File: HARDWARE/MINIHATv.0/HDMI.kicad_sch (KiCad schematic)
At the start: 3 parts, among them J3 HDMI_A, J4 DVI-D_Dual_Link, U4 TFP410PAP

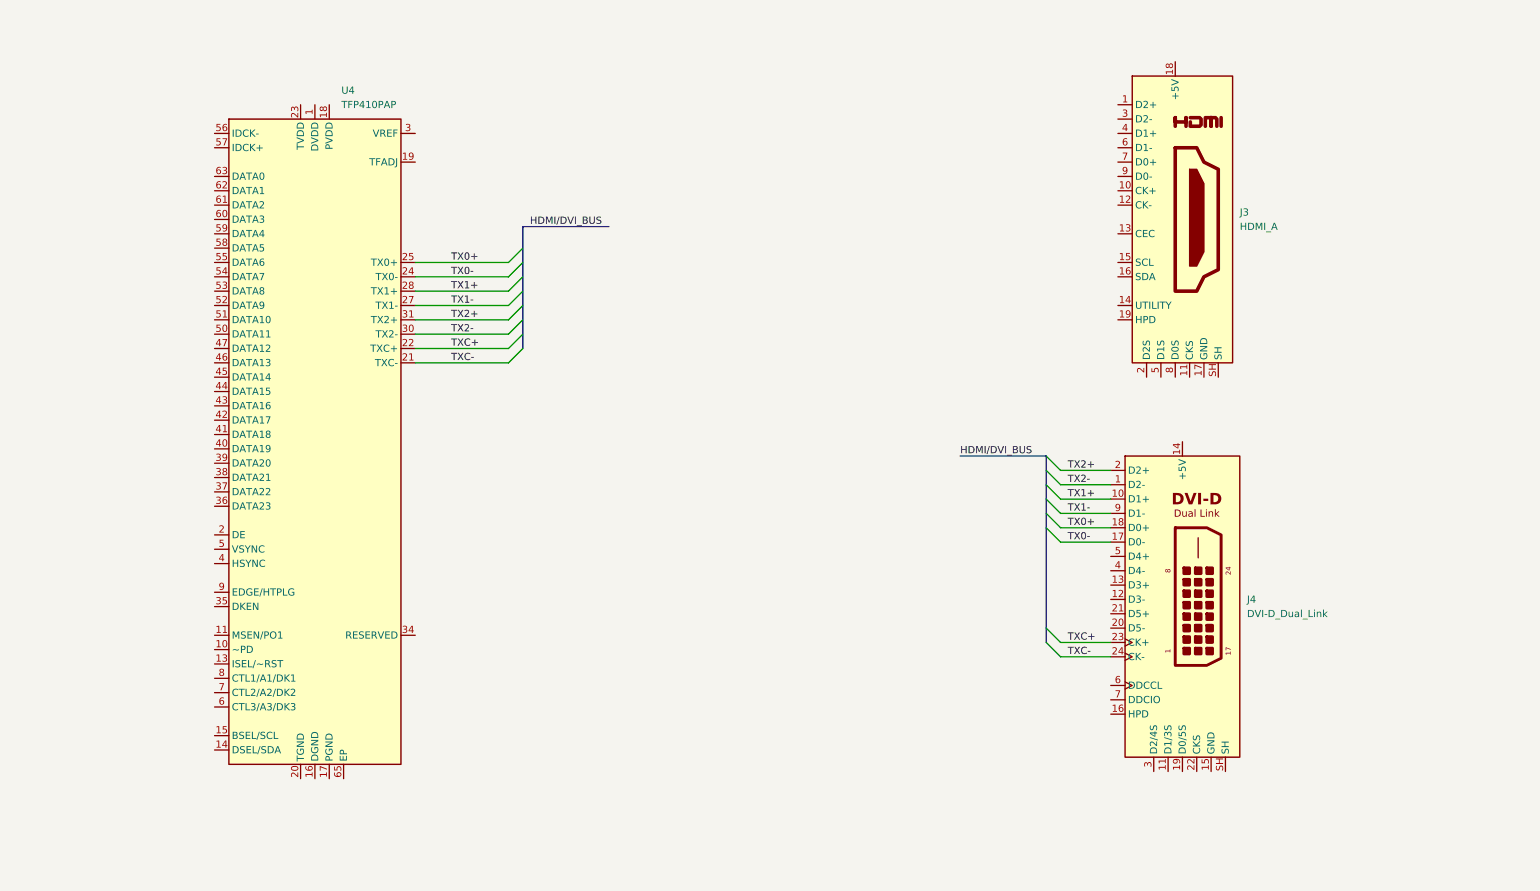
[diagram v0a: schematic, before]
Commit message: added beads and caps on drivers vdd
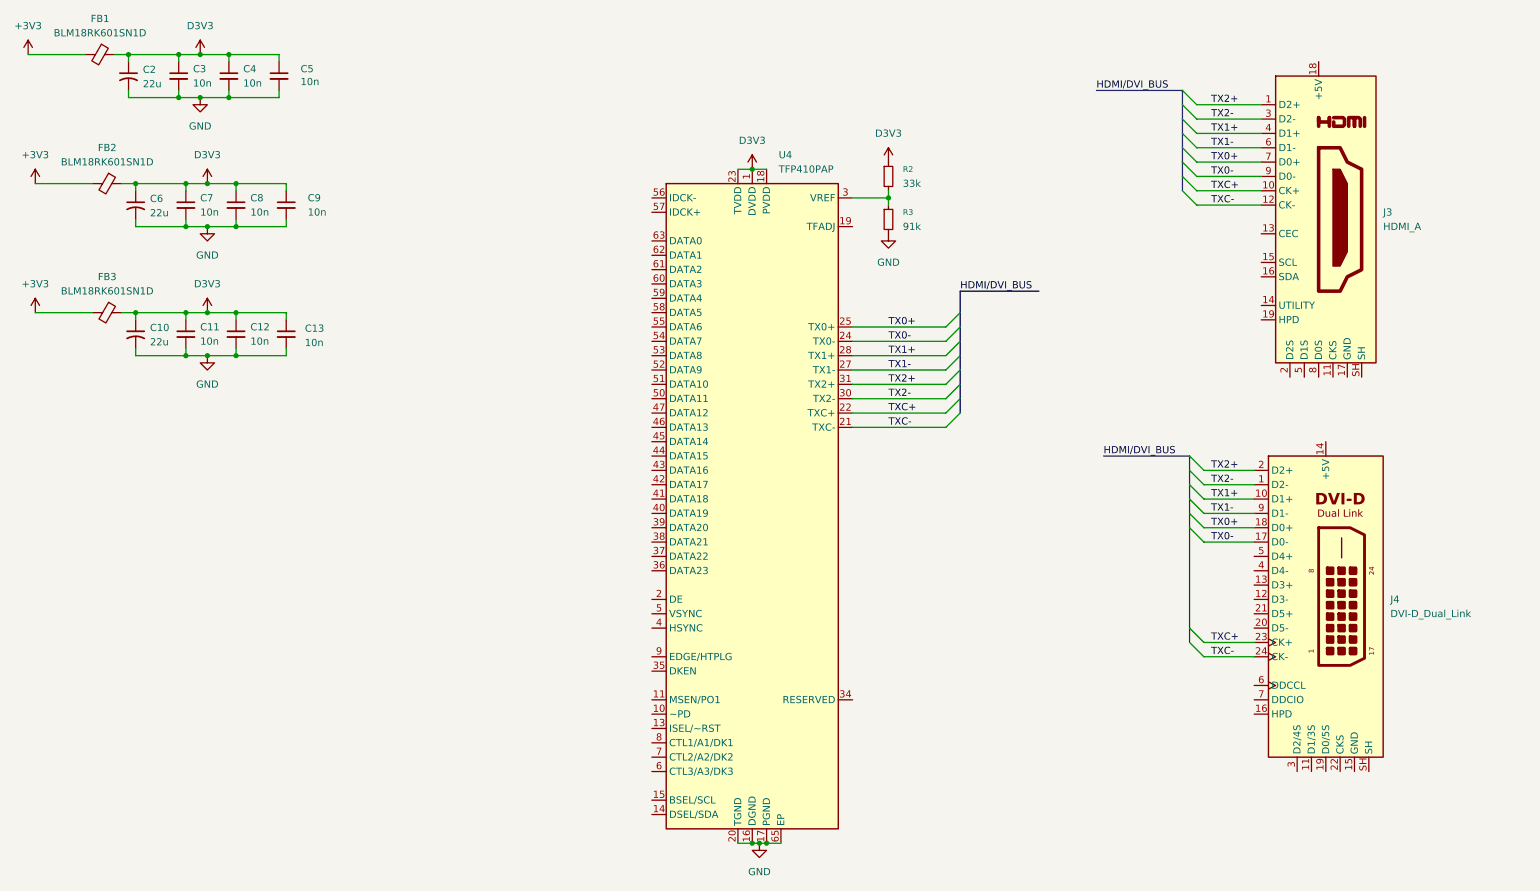
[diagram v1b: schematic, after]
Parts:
- added C10, C2, C6: 22u, symbol Device:C_Small_US
- added C11, C12, C13, C3, C4, C5, C7, C8, C9: 10n, symbol Device:C_Small
- added FB1, FB2, FB3: BLM18RK601SN1D, symbol Device:FerriteBead_Small
- added R2: 33k, symbol Device:R_Small
- added R3: 91k, symbol Device:R_Small
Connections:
- net TX0+: now also J3.7 (D0+)
- net TX0-: now also J3.9 (D0-)
- net TX1+: now also J3.4 (D1+)
- net TX1-: now also J3.6 (D1-)
- net TX2+: now also J3.1 (D2+)
- net TX2-: now also J3.3 (D2-)
- net TXC+: now also J3.10 (CK+)
- net TXC-: now also J3.12 (CK-)
- net D3V3: now reaches U4.1 (DVDD), U4.12 (DVDD), U4.33 (DVDD)
- net D3V3: now also U4.18 (PVDD), U4.23 (TVDD), U4.29 (TVDD), C10.1, C11.1, C12.1, C13.1, C2.1, C3.1, C4.1, C5.1, C6.1, C7.1, C8.1, C9.1, FB1.1, FB2.1, FB3.1, R2.1
- net GND: now reaches U4.16 (DGND), U4.48 (DGND), U4.64 (DGND)
- net GND: now also U4.17 (PGND), U4.20 (TGND), U4.26 (TGND), U4.32 (TGND), U4.65 (EP), C10.2, C11.2, C12.2, C13.2, C2.2, C3.2, C4.2, C5.2, C6.2, C7.2, C8.2, C9.2, R3.2
- net at U4.3 (VREF): now also R2.2, R3.1
- new net +3V3: FB1.2, FB2.2, FB3.2
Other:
- moved on the sheet: J3, J4, U4

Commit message: TFP to MCU connection added, TFP config pins tied
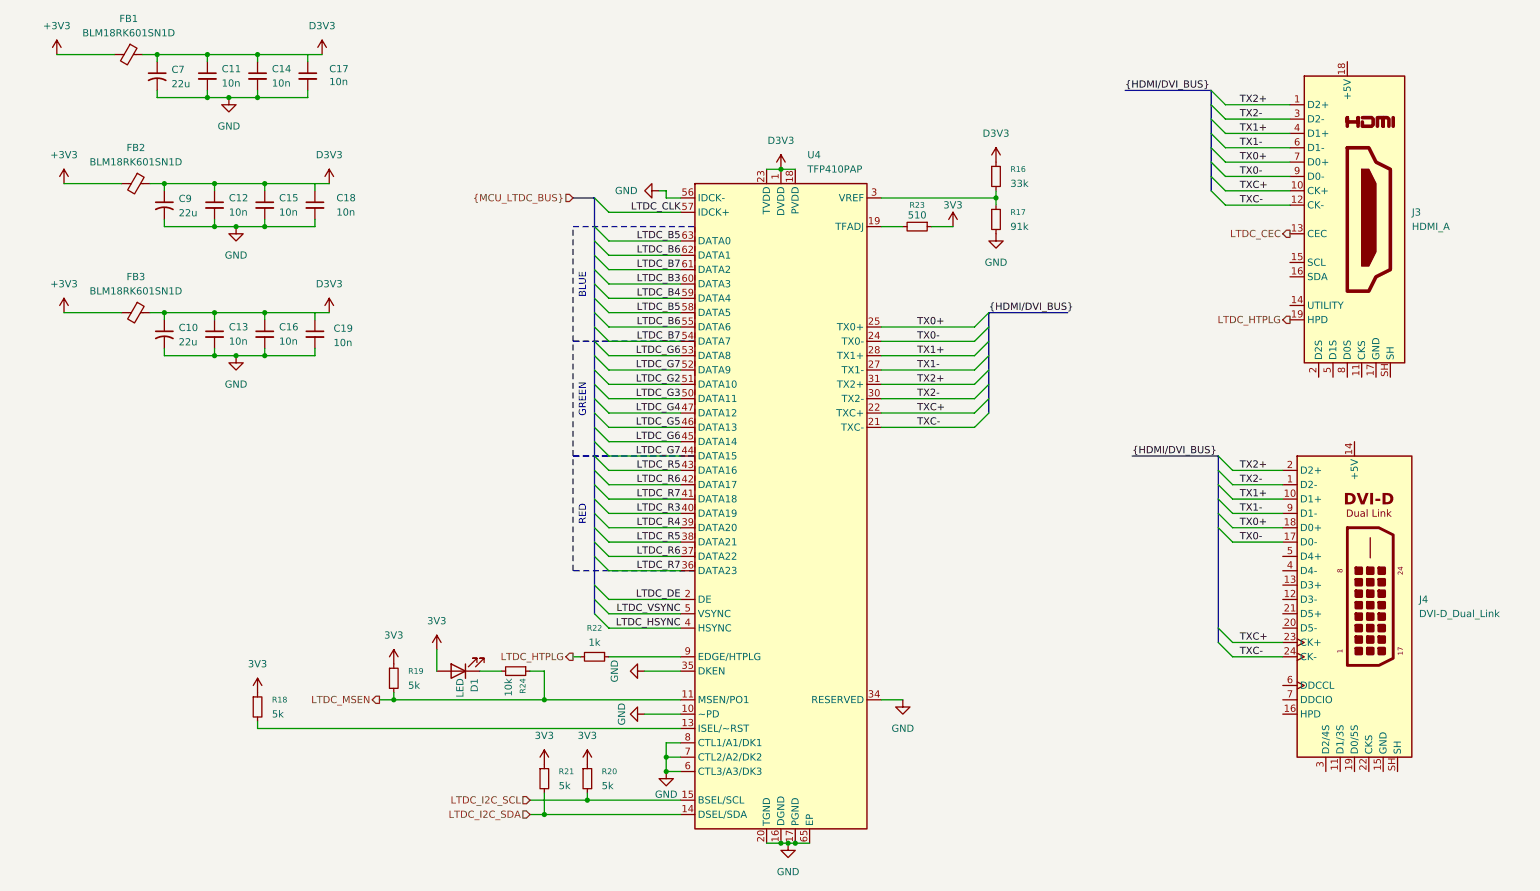
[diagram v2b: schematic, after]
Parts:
- added D1: LED, symbol Device:LED
- added R18, R19, R20, R21: 5k, symbol Device:R_Small
- added R22: 1k, symbol Device:R_Small
- added R23: 510, symbol Device:R_Small
- added R24: 10k, symbol Device:R_Small
- renumbered C3 to C11, C7 to C12, C11 to C13, C4 to C14, C8 to C15, C12 to C16, C5 to C17, C9 to C18, C13 to C19, C2 to C7, C6 to C9, R2 to R16, R3 to R17
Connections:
- net D3V3: no longer C17.1, C18.1, C19.1
- net GND: now also U4.10 (~PD), U4.34 (RESERVED), U4.35 (DKEN), U4.56 (IDCK-), U4.6 (CTL3/A3/DK3), U4.7 (CTL2/A2/DK2), U4.8 (CTL1/A1/DK1)
- net LTDC_MSEN: now reaches U4.11 (MSEN/PO1)
- net LTDC_MSEN: now also R19.2, R24.1
- net at U4.13 (ISEL/~RST): now also R18.2
- net LTDC_I2C_SDA: now reaches U4.14 (DSEL/SDA)
- net LTDC_I2C_SDA: now also R21.2
- net LTDC_I2C_SCL: now reaches U4.15 (BSEL/SCL)
- net LTDC_I2C_SCL: now also R20.2
- net at U4.19 (TFADJ): now also R23.2
- net LTDC_DE: now reaches U4.2 (DE)
- net LTDC_R7: now reaches U4.36 (DATA23)
- net LTDC_R7: now also U4.41 (DATA18)
- net LTDC_R6: now reaches U4.37 (DATA22)
- net LTDC_R6: now also U4.42 (DATA17)
- net LTDC_R5: now reaches U4.38 (DATA21)
- net LTDC_R5: now also U4.43 (DATA16)
- net LTDC_R4: now reaches U4.39 (DATA20)
- net LTDC_HSYNC: now reaches U4.4 (HSYNC)
- net LTDC_R3: now reaches U4.40 (DATA19)
- net LTDC_G7: now reaches U4.44 (DATA15)
- net LTDC_G7: now also U4.52 (DATA9)
- net LTDC_G6: now reaches U4.45 (DATA14)
- net LTDC_G6: now also U4.53 (DATA8)
- net LTDC_G5: now reaches U4.46 (DATA13)
- net LTDC_G4: now reaches U4.47 (DATA12)
- net LTDC_VSYNC: now reaches U4.5 (VSYNC)
- net LTDC_G3: now reaches U4.50 (DATA11)
- net LTDC_G2: now reaches U4.51 (DATA10)
- net LTDC_B7: now reaches U4.54 (DATA7)
- net LTDC_B7: now also U4.61 (DATA2)
- net LTDC_B6: now reaches U4.55 (DATA6)
- net LTDC_B6: now also U4.62 (DATA1)
- net LTDC_CLK: now reaches U4.57 (IDCK+)
- net LTDC_B5: now reaches U4.58 (DATA5)
- net LTDC_B5: now also U4.63 (DATA0)
- net LTDC_B4: now reaches U4.59 (DATA4)
- net LTDC_B3: now reaches U4.60 (DATA3)
- net at U4.9 (EDGE/HTPLG): now also R22.1
- net LTDC_CEC: now reaches J3.13 (CEC)
- net LTDC_HTPLG: now reaches J3.19 (HPD)
- net LTDC_HTPLG: now also R22.2
- new net: D1.1 (K), R24.2
- new net 3V3: D1.2 (A), R18.1, R19.1, R20.1, R21.1, R23.1
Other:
- moved on the sheet: C10, C11, C12, C13, C14, C15, C16, C17, C18, C19, C7, C9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

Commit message: deleted DVI, LTDC LSB tied GND
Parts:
- removed J4: DVI-D_Dual_Link, symbol Connector:DVI-D_Dual_Link
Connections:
- net GND: now also J3.17 (GND), J3.SH, U4.41 (DATA18), U4.42 (DATA17), U4.43 (DATA16), U4.52 (DATA9), U4.53 (DATA8), U4.61 (DATA2), U4.62 (DATA1), U4.63 (DATA0)
- net LTDC_B5: no longer U4.63 (DATA0)
- net LTDC_B6: no longer U4.62 (DATA1)
- net LTDC_B7: no longer U4.61 (DATA2)
- net LTDC_G6: no longer U4.53 (DATA8)
- net LTDC_G7: no longer U4.52 (DATA9)
- net LTDC_R5: no longer U4.43 (DATA16)
- net LTDC_R6: no longer U4.42 (DATA17)
- net LTDC_R7: no longer U4.41 (DATA18)
- net 5V: now reaches J3.18 (+5V)
- no-connect marks 0 -> 1
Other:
- moved on the sheet: J3

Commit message: HDMI socked connection finished
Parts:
- R24: value 10k -> 120
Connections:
- net GND: now also J3.11 (CKS), J3.2 (D2S), J3.5 (D1S), J3.8 (D0S)
- net HDMI_SCL: now reaches J3.15 (SCL)
- net HDMI_SDA: now reaches J3.16 (SDA)
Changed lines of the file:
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@@
 	)
 	(junction
-		(at 265.43 121.92)
-		(diameter 0)
-		(color 0 0 0 0)
-	)
-	(junction
 		(at 53.34 55.88)
 		(diameter 0)
@@
 	)
 	(junction
+		(at 259.08 121.92)
+		(diameter 0)
+		(color 0 0 0 0)
+	)
+	(junction
 		(at 60.96 33.02)
 		(diameter 0)
@@
 	)
 	(junction
+		(at 264.16 121.92)
+		(diameter 0)
+		(color 0 0 0 0)
+	)
+	(junction
+		(at 256.54 121.92)
+		(diameter 0)
+		(color 0 0 0 0)
+	)
+	(junction
 		(at 62.23 48.26)
 		(diameter 0)
@@
 	)
 	(junction
+		(at 260.35 121.92)
+		(diameter 0)
+		(color 0 0 0 0)
+	)
+	(junction
 		(at 111.76 160.02)
 		(diameter 0)
@@
 	)
 	(junction
+		(at 261.62 121.92)
+		(diameter 0)
+		(color 0 0 0 0)
+	)
+	(junction
 		(at 135.89 78.74)
 		(diameter 0)
@@
 	(wire
 		(pts
+			(xy 259.08 121.92) (xy 260.35 121.92)
+		)
+		(stroke
+			(width 0)
+			(type default)
+		)
+	)
+	(wire
+		(pts
 			(xy 119.38 157.48) (xy 135.89 157.48)
 		)
@@
 	(wire
 		(pts
+			(xy 254 121.92) (xy 256.54 121.92)
+		)
+		(stroke
+			(width 0)
+			(type default)
+		)
+	)
+	(wire
+		(pts
 			(xy 60.96 143.51) (xy 60.96 144.78)
 		)
@@
 	(wire
 		(pts
-			(xy 264.16 121.92) (xy 265.43 121.92)
-		)
-		(stroke
-			(width 0)
-			(type default)
-		)
-	)
-	(wire
-		(pts
-			(xy 265.43 121.92) (xy 266.7 121.92)
-		)
-		(stroke
-			(width 0)
-			(type default)
-		)
-	)
-	(wire
-		(pts
 			(xy 111.76 134.62) (xy 111.76 139.7)
 		)
@@
 	(wire
 		(pts
+			(xy 234.95 111.76) (xy 248.92 111.76)
+		)
+		(stroke
+			(width 0)
+			(type default)
+		)
+	)
+	(wire
+		(pts
 			(xy 171.45 76.2) (xy 187.96 76.2)
 		)
@@
 	(wire
 		(pts
+			(xy 260.35 121.92) (xy 266.7 121.92)
+		)
+		(stroke
+			(width 0)
+			(type default)
+		)
+	)
+	(wire
+		(pts
+			(xy 260.35 124.46) (xy 260.35 121.92)
+		)
+		(stroke
+			(width 0)
+			(type default)
+		)
+	)
+	(wire
+		(pts
 			(xy 135.89 50.8) (xy 133.35 50.8)
 		)
@@
 	(wire
 		(pts
+			(xy 256.54 121.92) (xy 259.08 121.92)
+		)
+		(stroke
+			(width 0)
+			(type default)
+		)
+	)
+	(wire
+		(pts
 			(xy 123.19 106.68) (xy 135.89 106.68)
 		)
@@
 	)
 	(label "LTDC_HTPLG"
-		(at 248.92 111.76 180)
+		(at 234.95 111.76 0)
 		(effects
 			(font
 				(size 1.27 1.27)
 			)
-			(justify right bottom)
+			(justify left bottom)
 		)
 	)
@@
 		)
 	)
+	(hierarchical_label "HDMI_SDA"
+		(shape output)
+		(at 248.92 104.14 180)
+		(effects
+			(font
+				(size 1.27 1.27)
+			)
+			(justify right)
+		)
+	)
 	(hierarchical_label "{MCU_LTDC_BUS}"
 		(shape input)
@@
 		)
 	)
+	(hierarchical_label "HDMI_SCL"
+		(shape output)
+		(at 248.92 101.6 180)
+		(effects
+			(font
+				(size 1.27 1.27)
+			)
+			(justify right)
+		)
+	)
 	(hierarchical_label "LTDC_I2C_SDA"
 		(shape input)
@@
 			)
 		)
-		(property "Value" "10k"
+		(property "Value" "120"
 			(at 105.41 135.89 0)
 			(show_name no)
@@
 	(symbol
 		(lib_id "power:GND")
-		(at 265.43 121.92 0)
+		(at 260.35 124.46 0)
 		(unit 1)
 		(body_style 1)
@@
 		(fields_autoplaced yes)
 		(property "Reference" "#PWR033"
-			(at 265.43 128.27 0)
+			(at 260.35 130.81 0)
 			(hide yes)
 			(show_name no)
@@
 		)
 		(property "Value" "GND"
-			(at 265.43 127 0)
+			(at 260.35 129.54 0)
 			(show_name no)
 			(do_not_autoplace no)
@@
 		)
 		(property "Footprint" ""
-			(at 265.43 121.92 0)
+			(at 260.35 124.46 0)
 			(hide yes)
 			(show_name no)
@@
 		)
 		(property "Datasheet" ""
-			(at 265.43 121.92 0)
+			(at 260.35 124.46 0)
 			(hide yes)
 			(show_name no)
@@
 		)
 		(property "Description" "Power symbol creates a global label with name \"GND\" , ground"
-			(at 265.43 121.92 0)
+			(at 260.35 124.46 0)
 			(hide yes)
 			(show_name no)

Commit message: added i2c for hdmi
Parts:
- D7: renamed from D1; value LED -> LED B
- renumbered C7 to C21, C9 to C22, C10 to C23, C11 to C24, C12 to C25, C13 to C26, C14 to C27, C15 to C28, C16 to C29, C17 to C30, C18 to C31, C19 to C32, FB1 to FB2, FB2 to FB3, FB3 to FB4, J3 to J4, R18 to R29, R19 to R30, R24 to R31, R21 to R32, R20 to R33, R22 to R34, R23 to R35, R16 to R36, R17 to R37, U4 to U6
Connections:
- net 5V renamed +5V

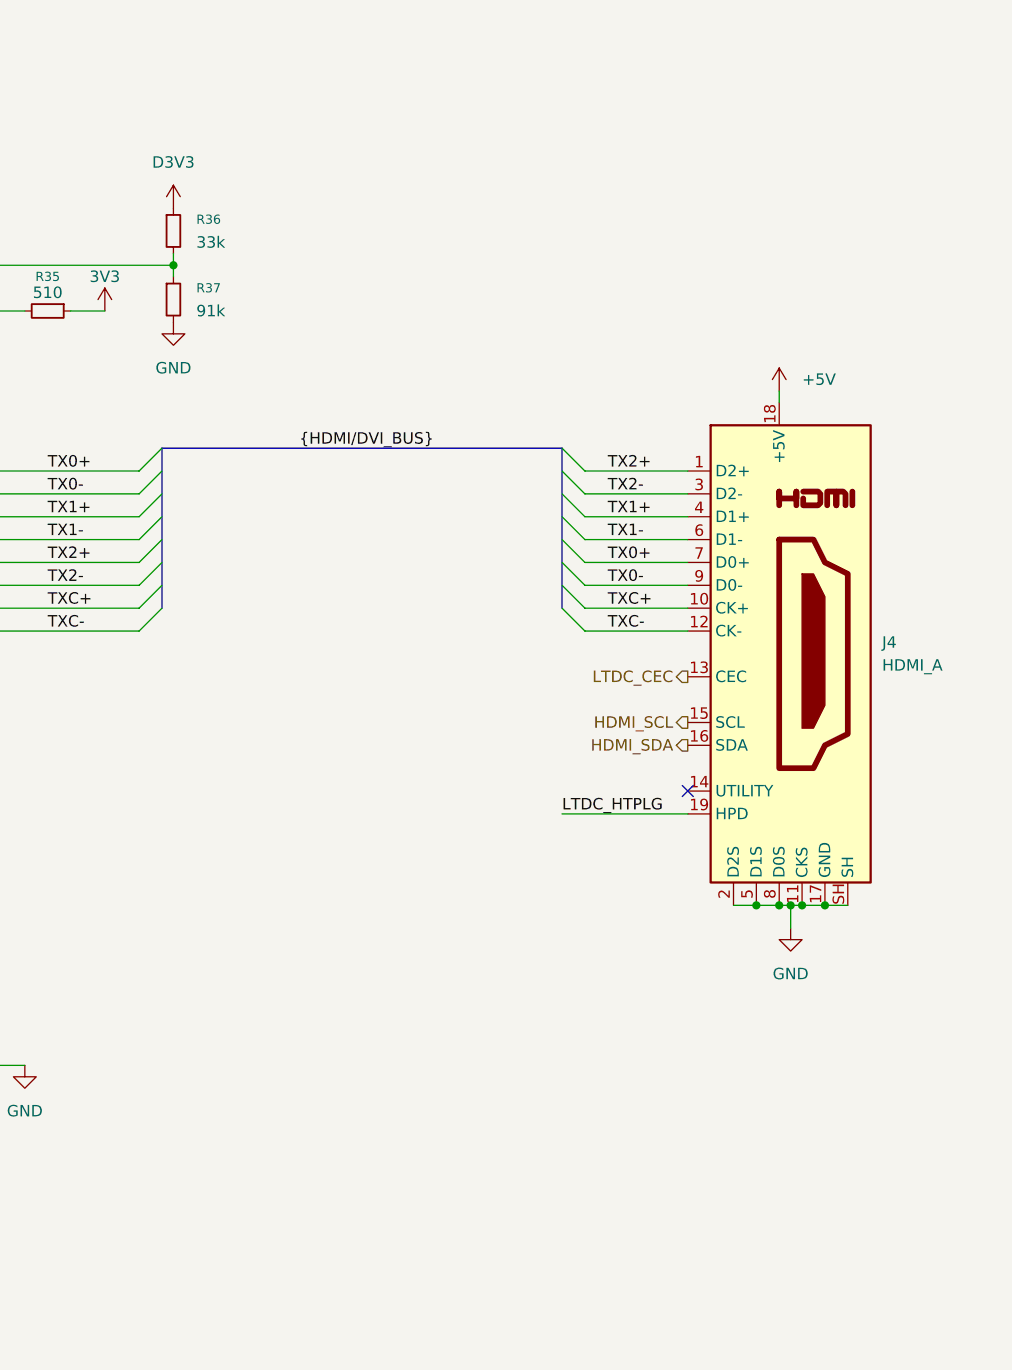
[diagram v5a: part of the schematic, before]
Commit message: connecting i2c and uart bt/hdmi
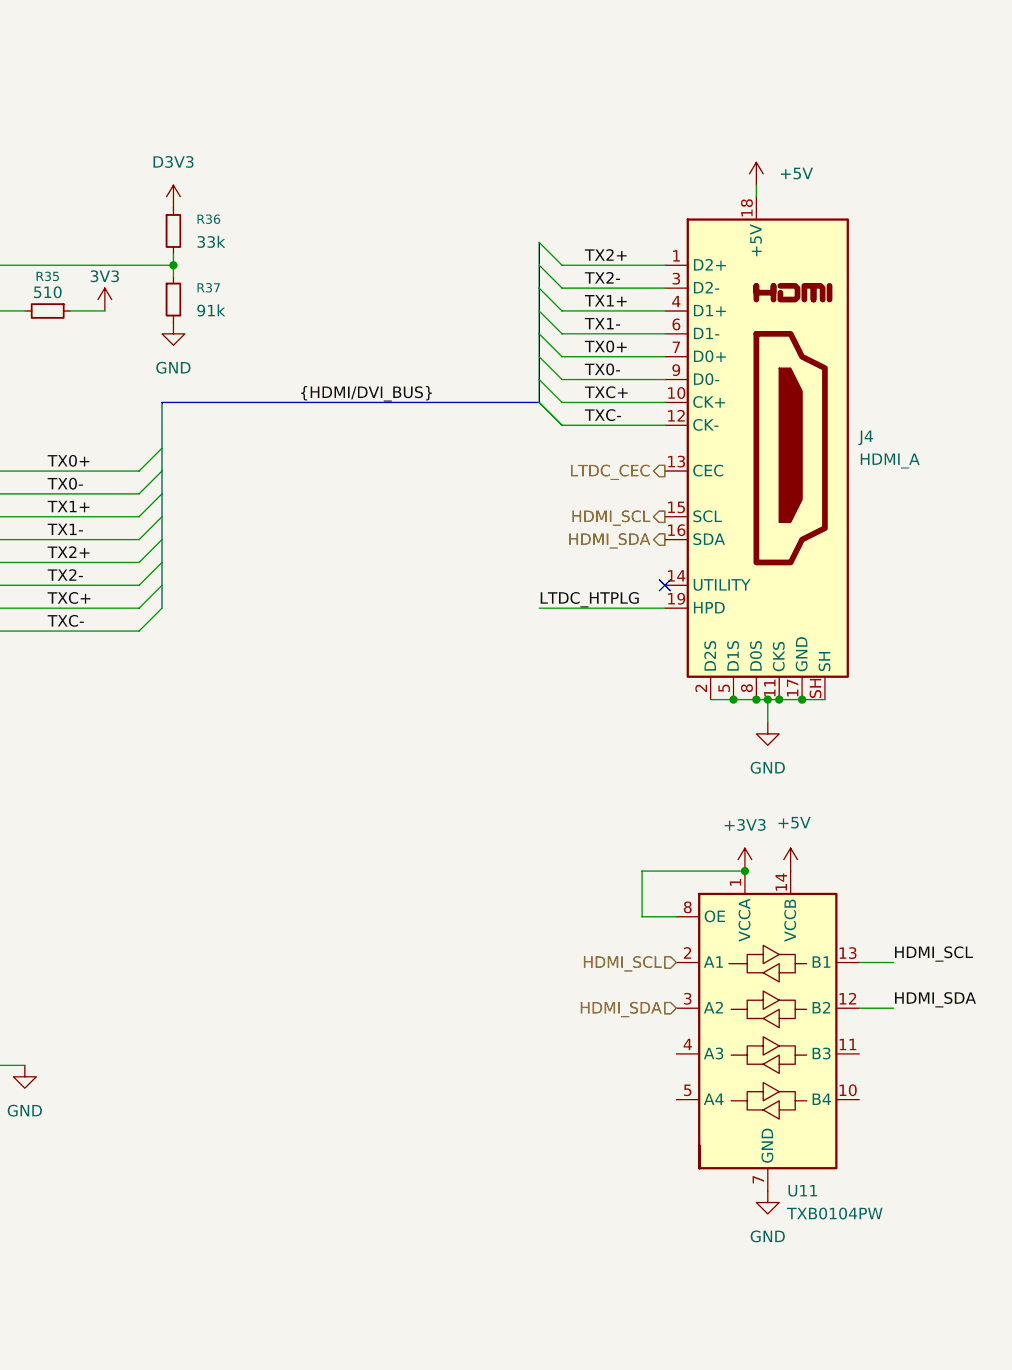
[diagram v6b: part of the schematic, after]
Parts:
- added U11: TXB0104PW, Package_SO:TSSOP-14_4.4x5mm_P0.65mm, symbol Logic_LevelTranslator:TXB0104PW
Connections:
- net +3V3: now also U11.1 (VCCA), U11.8 (OE)
- net +5V: now also U11.14 (VCCB)
- net GND: now also U11.7 (GND)
- net HDMI_SCL: now also U11.13 (B1), U11.2 (A1)
- net HDMI_SDA: now also U11.12 (B2), U11.3 (A2)
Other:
- moved on the sheet: J4
